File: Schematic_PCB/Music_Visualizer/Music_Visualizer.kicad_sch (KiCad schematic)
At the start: 130 parts, among them J1 AudioJack2_Ground, SW1 SW_SPDT, U1 LM324, U2 LM324, U3 LM324, U4 LM324, U5 LM324, U6 LM324

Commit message: Got 3D models for all parts, corrected signal voltage to each driver and made outline of PCB
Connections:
- net GND: now also J1.G
- net Vsig_female: now also J1.T, SW1.3 (C)
- net at U6.12 (+): now also U6.14
- net at U6.13 (-): now also U6.6 (-), U6.9 (-)
- net at U6.5 (+): now also U6.7
- net at U6.10 (+): now also U6.8
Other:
- moved on the sheet: J1, JP1, SW1, U6B, U6C, U6D

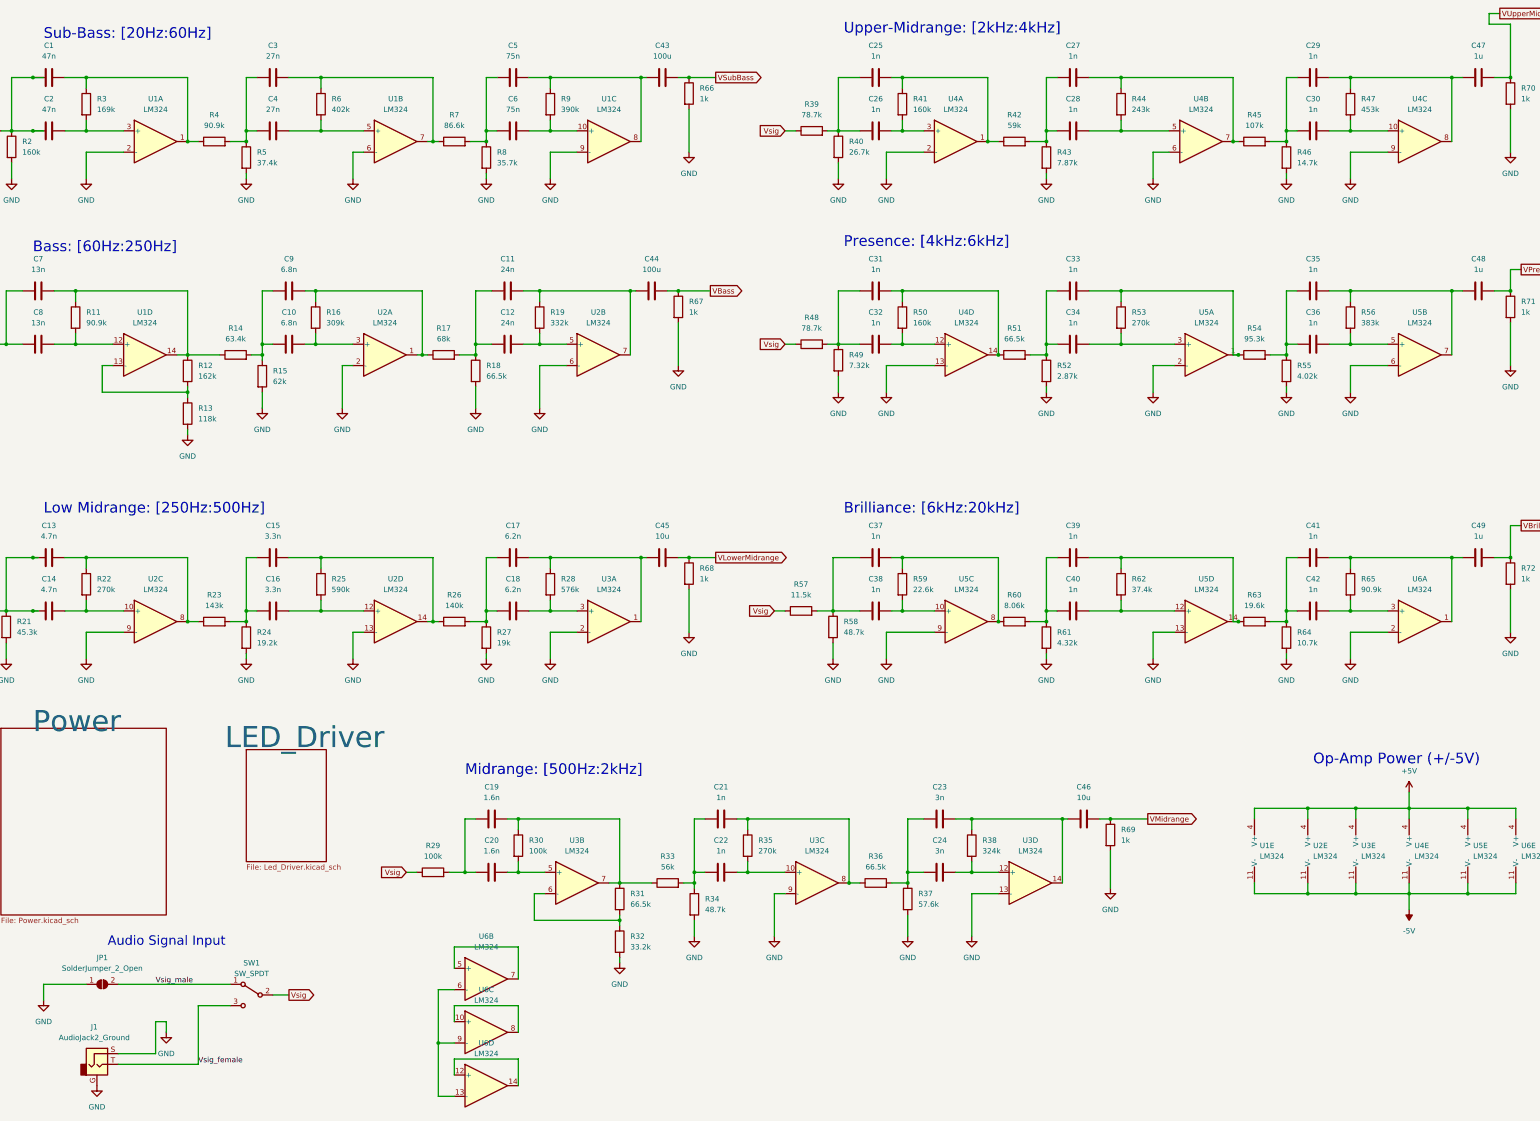
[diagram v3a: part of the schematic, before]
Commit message: Added 7th LM324 Quad-op-amp IC to Filter array, updated numbering on all other ICs
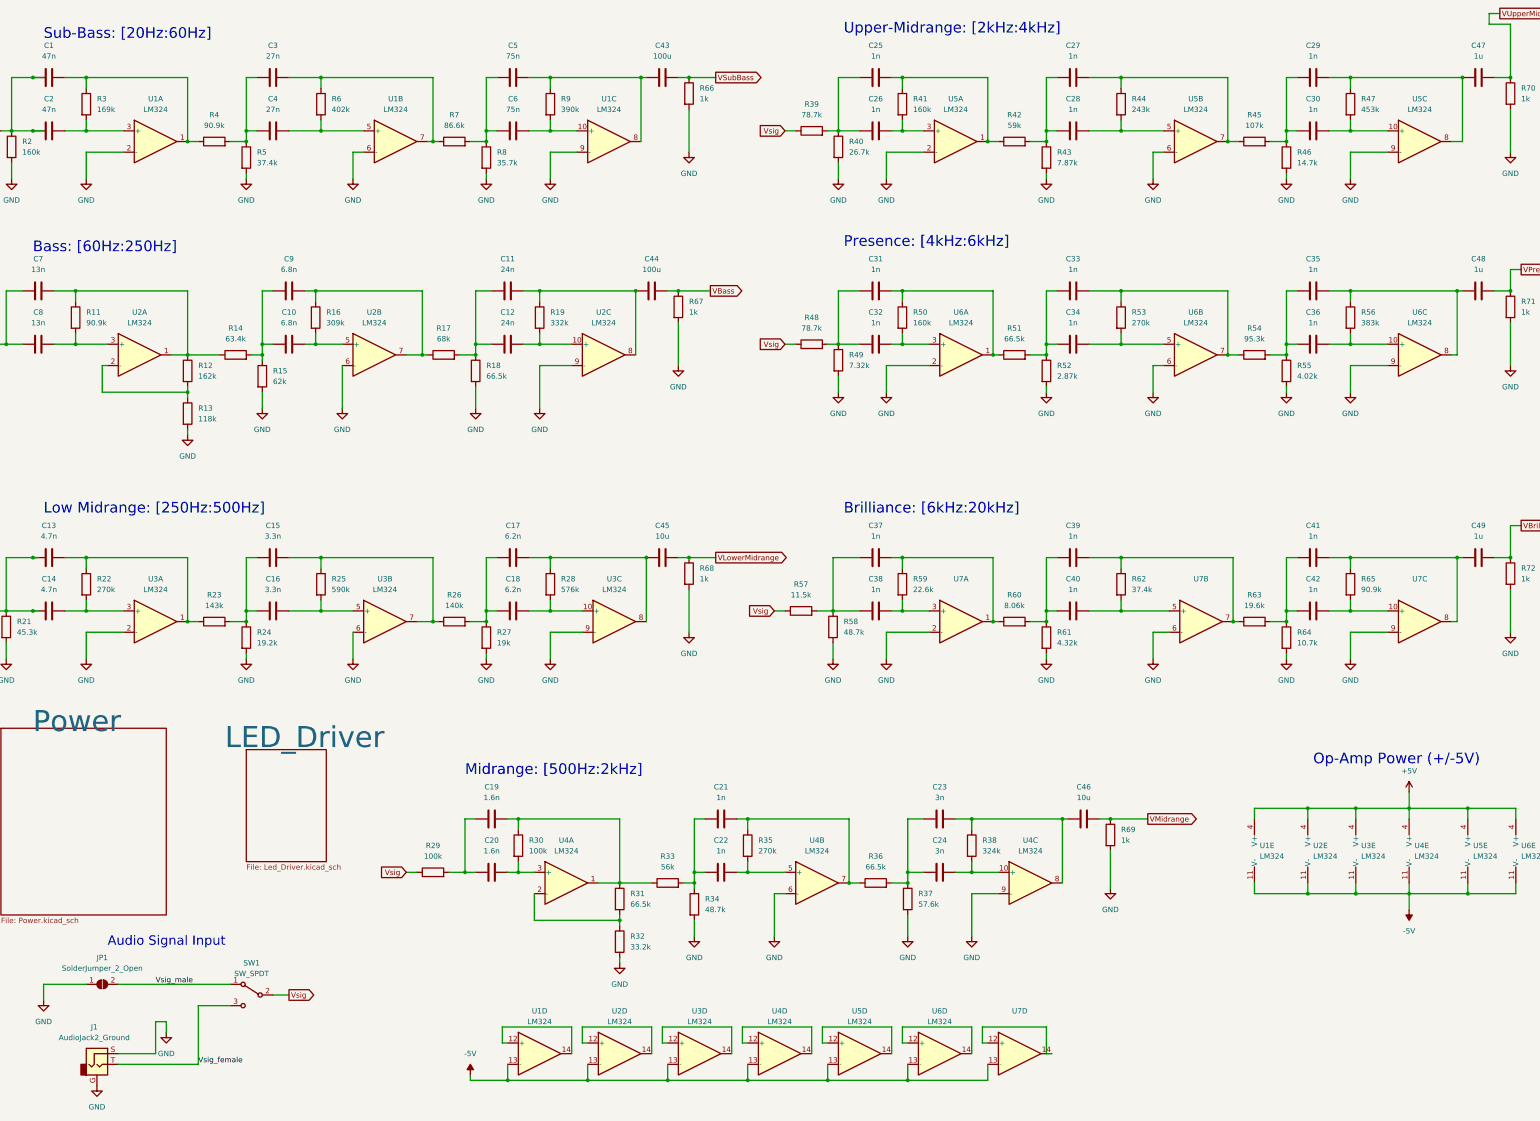
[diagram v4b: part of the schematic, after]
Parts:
- added U7: (no value), symbol Amplifier_Operational:LM324
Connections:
- net -5V: now also U1.13 (-), U2.13 (-), U3.13 (-), U4.13 (-), U5.13 (-), U6.13 (-), U7.13 (-)
- net GND: now also U3.6 (-), U6.6 (-), U6.9 (-), U7.2 (-), U7.6 (-), U7.9 (-); no longer U2.13 (-), U2.2 (-), U3.13 (-), U4.13 (-), U4.2 (-), U5.13 (-)
- net at C15.2, R25.1, R26.1: now also U3.7; no longer U2.14
- net at C38.2, R59.2: now also U7.3 (+); no longer U5.10 (+)
- net at C37.2, R59.1, R60.1: now also U7.1; no longer U5.8
- net at C23.2, C46.1, R38.1: now also U4.8; no longer U3.14
- net at C7.2, R11.1, R12.1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: now also U2.1; no longer U1.14
- net at C36.2, R56.2: now also U6.10 (+); no longer U5.5 (+)
- net at C11.2, C44.1, R19.1: now also U2.8; no longer U2.7
- net at C41.2, C49.1, R65.1: now also U7.8; no longer U6.1
- net at C42.2, R65.2: now also U7.10 (+); no longer U6.3 (+)
- net at C20.2, R30.2: now also U4.3 (+); no longer U3.5 (+)
- net at R31.2, R32.1: now also U4.2 (-); no longer U3.6 (-)
- net at C19.2, R30.1, R31.1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: now also U4.1; no longer U3.7
- net at C8.2, R11.2: now also U2.3 (+); no longer U1.12 (+)
- net at R12.2, R13.1: now also U2.2 (-); no longer U1.13 (-)
- net at C33.2, R53.1, R54.1: now also U6.7; no longer U5.1
- net at C34.2, R53.2: now also U6.5 (+); no longer U5.3 (+)
- net at C13.2, R22.1, R23.1: now also U3.1; no longer U2.8
- net at C14.2, R22.2: now also U3.3 (+); no longer U2.10 (+)
- net at C40.2, R62.2: now also U7.5 (+); no longer U5.12 (+)
- net at C39.2, R62.1, R63.1: now also U7.7; no longer U5.14
- net at C27.2, R44.1, R45.1: now also U5.7; no longer U4.7
- net at C12.2, R19.2: now also U2.10 (+); no longer U2.5 (+)
- net at C35.2, C48.1, R56.1: now also U6.8; no longer U5.7
- net at C17.2, C45.1, R28.1: now also U3.8; no longer U3.1
- net at C28.2, R44.2: now also U5.5 (+); no longer U4.5 (+)
- net at C25.2, R41.1, R42.1: now also U5.1; no longer U4.1
- net at C26.2, R41.2: now also U5.3 (+); no longer U4.3 (+)
- net at C9.2, R16.1, R17.1: now also U2.7; no longer U2.1
- net at C29.2, C47.1, R47.1: now also U5.8; no longer U4.8
- net at C30.2, R47.2: now also U5.10 (+); no longer U4.10 (+)
- net at C10.2, R16.2: now also U2.5 (+); no longer U2.3 (+)
- net at C24.2, R38.2: now also U4.10 (+); no longer U3.12 (+)
- net at C31.2, R50.1, R51.1: now also U6.1; no longer U4.14
- net at C18.2, R28.2: now also U3.10 (+); no longer U3.3 (+)
- net at C32.2, R50.2: now also U6.3 (+); no longer U4.12 (+)
- net at C22.2, R35.2: now also U4.5 (+); no longer U3.10 (+)
- net at C21.2, R35.1, R36.1: now also U4.7; no longer U3.8
- net at C16.2, R25.2: now also U3.5 (+); no longer U2.12 (+)
- new net: U1.12 (+), U1.14
- new net: U5.12 (+), U5.14
- new net: U4.12 (+), U4.14
- new net: U3.12 (+), U3.14
- new net: U7.12 (+), U7.14
- new net: U2.12 (+), U2.14
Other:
- moved on the sheet: U1D, U2A, U2B, U2C, U2D, U3A, U3B, U3C, U3D, U4A, U4B, U4C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

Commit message: Routed bass and sub-bass
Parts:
- added unit 5 of U7
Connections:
- net +5V: now also U7.4 (V+)
- net -5V: now also U7.11 (V-); no longer U1.13 (-), U2.13 (-), U3.13 (-), U4.13 (-), U5.13 (-), U6.13 (-), U7.13 (-)
- net at U1.12 (+): no longer U1.14
- net at U6.12 (+): no longer U6.14
- net at U5.12 (+): no longer U5.14
- net at U4.12 (+): no longer U4.14
- net at U3.12 (+): no longer U3.14
- net at U7.12 (+): no longer U7.14
- net at U2.12 (+): no longer U2.14
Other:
- moved on the sheet: U1E, U2E, U3E, U4E, U5E, U6E
